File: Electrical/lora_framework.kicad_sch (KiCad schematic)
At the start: 21 parts, among them J1 Conn_Coaxial_Small, P1 USB_C_Plug_USB2.0, SW1 SW_Push, SW2 SW_Push, U1 E22-400MM22S, U2 STM32F042F6Px, U3 TLV76733DRVR

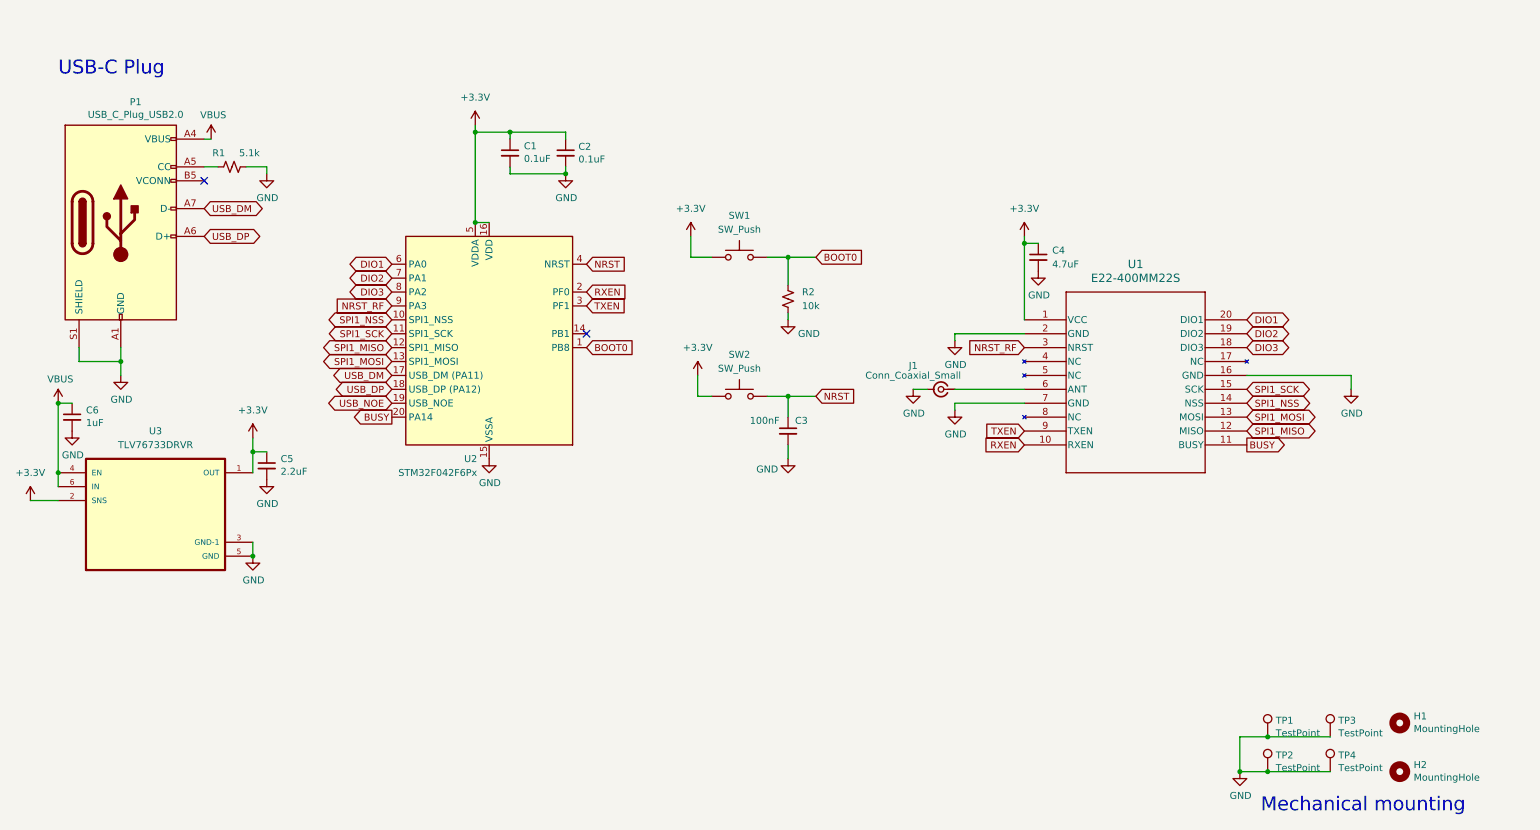
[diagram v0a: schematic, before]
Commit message: swapped USB connector for easier assemb
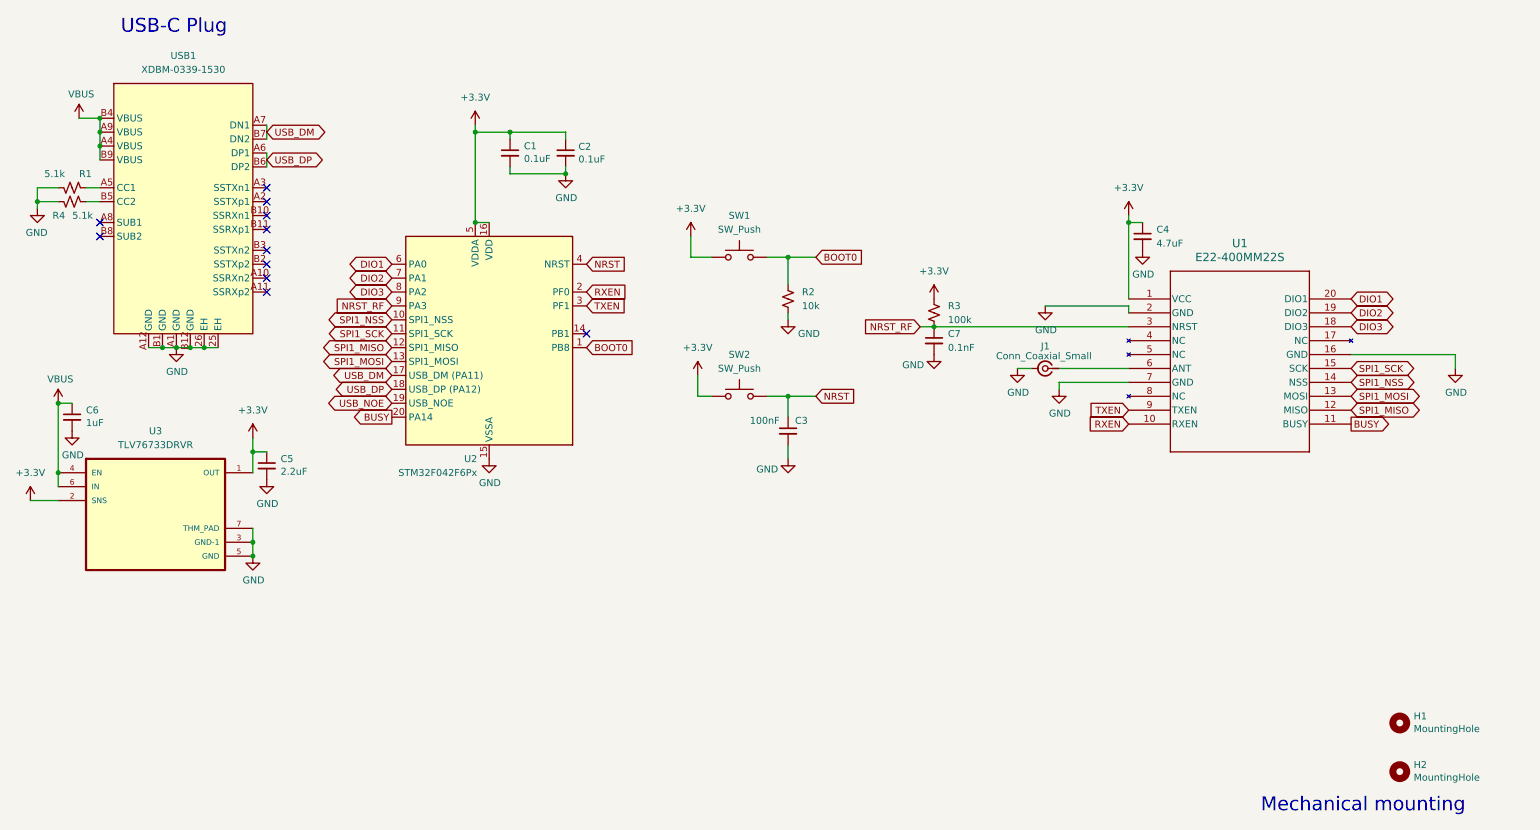
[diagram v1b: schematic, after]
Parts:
- removed P1: USB_C_Plug_USB2.0, Connector_USB:USB_C_Plug_Molex_105444, symbol Connector:USB_C_Plug_USB2.0
- removed TP1, TP2, TP3, TP4: TestPoint, TestPoint:TestPoint_Pad_1.5x1.5mm, symbol Connector:TestPoint
- added C7: 0.1nF, Capacitor_SMD:C_0402_1005Metric, symbol Device:C_Small
- added R3: 100k, Resistor_SMD:R_0402_1005Metric, symbol Device:R_Small_US
- added R4: 5.1k, Resistor_SMD:R_0402_1005Metric, symbol Device:R_Small_US
- added USB1: XDBM-0339-1530, footprints:USB-C-SMD_USB-3.1-C-TYPE, symbol XDBM-0339-1530:XDBM-0339-1530
- SW1, SW2: footprint Button_Switch_SMD:SW_SPST_B3U-3000P-B -> Button_Switch_SMD:SW_Push_SPST_NO_Alps_SKRK
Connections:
- net +3.3V: now also R3.1
- net GND: now also U3.7 (THM_PAD), C7.2, R4.1, USB1.25 (EH), USB1.26 (EH), USB1.A1 (GND), USB1.A12 (GND), USB1.B1 (GND), USB1.B12 (GND)
- net NRST_RF: now also C7.1, R3.2
- net USB_DM: now also USB1.A7 (DN1), USB1.B7 (DN2)
- net USB_DP: now also USB1.A6 (DP1), USB1.B6 (DP2)
- net VBUS: now also USB1.A4 (VBUS), USB1.A9 (VBUS), USB1.B4 (VBUS), USB1.B9 (VBUS)
- net at R1.1: now also USB1.A5 (CC1)
- new net: R4.2, USB1.B5 (CC2)
- no-connect marks 2 -> 11
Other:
- moved on the sheet: C4, J1, R1, U1
